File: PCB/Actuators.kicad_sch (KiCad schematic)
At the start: 90 parts, among them J1 R_Motor, J10 Servos, J11 PWR-Servos, J3 Left_Speaker, J4 Right_Speaker, J5 GAIN_sel, J6 L_Motor, J7 Servos, J8 Servos, J9 Servos, Q1 AOD417, U10 BTN7960B, U11 PCA9685PW, U2 MAX98357A, U4 MAX98357A, U5 BTN7960B, U6 BTN7960B, U7 74HC244, U8 74HC244, U9 BTN7960B

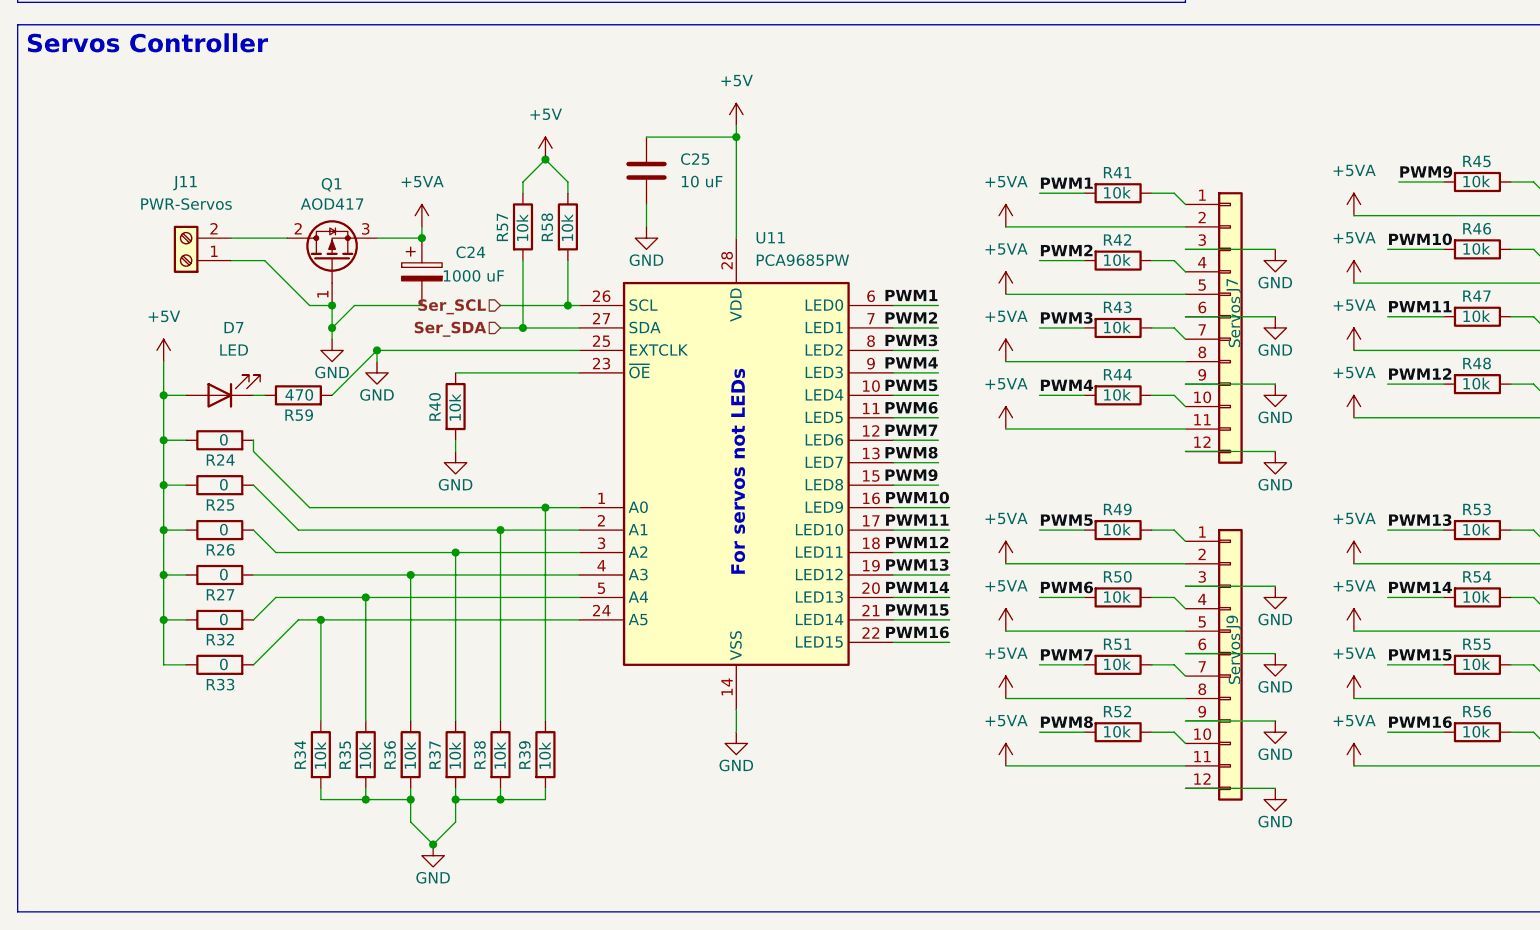
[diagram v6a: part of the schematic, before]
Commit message: [PCB] Traced motors controllers & step downs
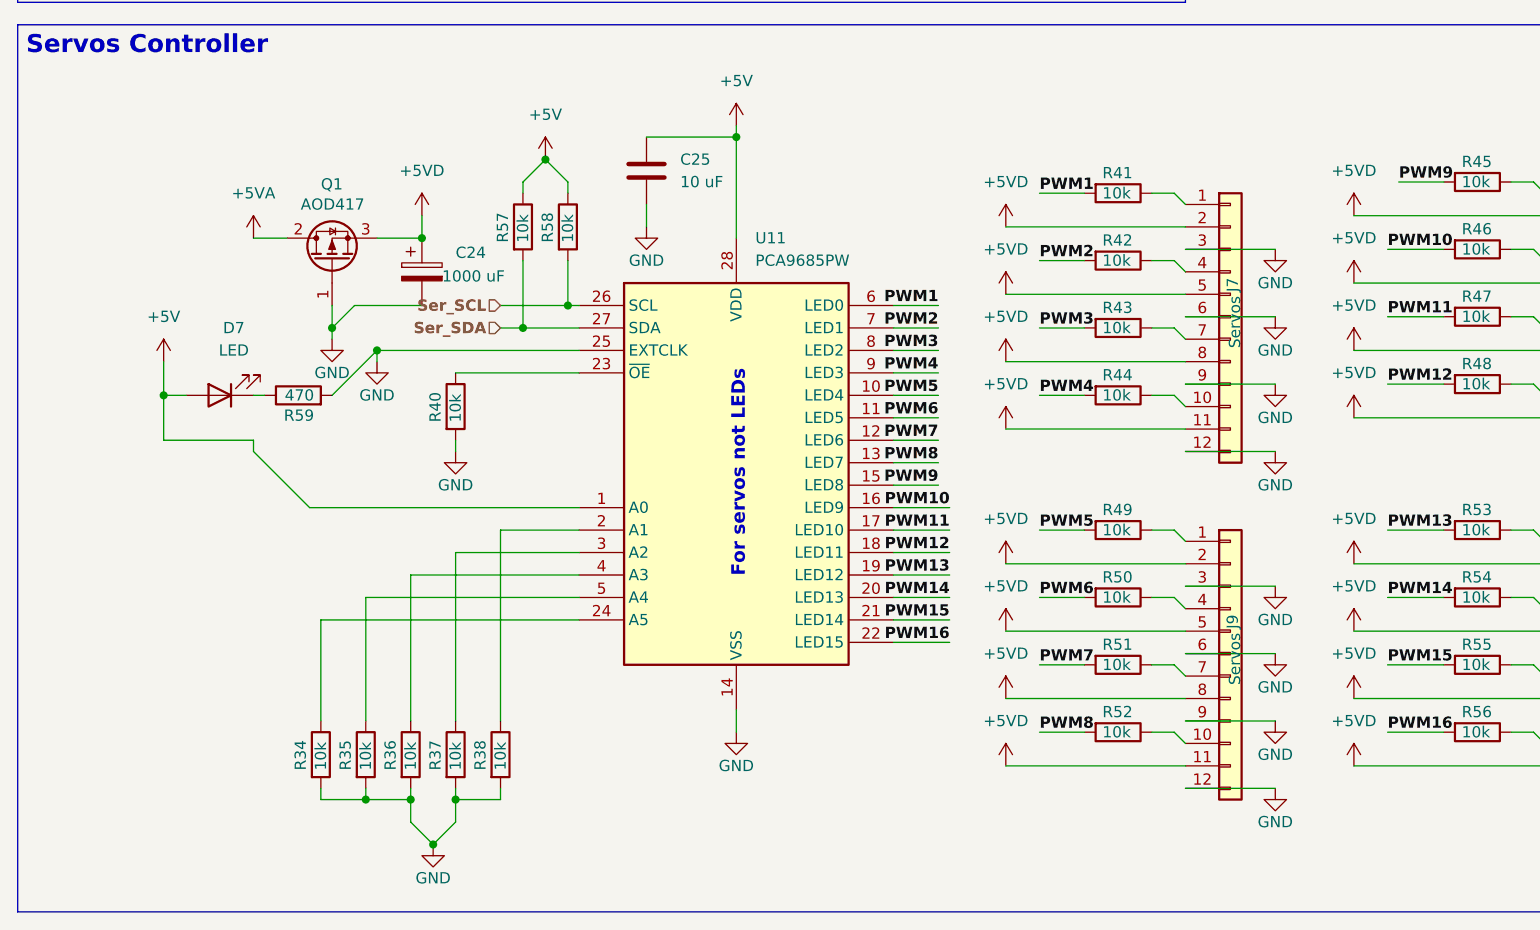
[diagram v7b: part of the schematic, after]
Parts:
- removed J11: PWR-Servos, TerminalBlock_Altech:Altech_AK100_1x02_P5.00mm, symbol Connector:Screw_Terminal_01x02
- removed R24, R25, R26, R27, R32, R33: 0, Resistor_SMD:R_0603_1608Metric_Pad0.98x0.95mm_HandSolder, symbol Device:R
- removed R39: 10k, Resistor_SMD:R_0603_1608Metric_Pad0.98x0.95mm_HandSolder, symbol Device:R
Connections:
- net +5V: now also U11.1 (A0)
- net +5VA: now also Q1.2 (D); no longer C24.1, J10.11 (Pin_11), J10.2 (Pin_2), J10.5 (Pin_5), J10.8 (Pin_8), J7.11 (Pin_11), J7.2 (Pin_2), J7.5 (Pin_5), J7.8 (Pin_8), J8.11 (Pin_11), J8.2 (Pin_2), J8.5 (Pin_5), J8.8 (Pin_8), J9.11 (Pin_11), J9.2 (Pin_2), J9.5 (Pin_5), J9.8 (Pin_8), Q1.3 (S)
- new net +5VD: C24.1, J10.11 (Pin_11), J10.2 (Pin_2), J10.5 (Pin_5), J10.8 (Pin_8), J7.11 (Pin_11), J7.2 (Pin_2), J7.5 (Pin_5), J7.8 (Pin_8), J8.11 (Pin_11), J8.2 (Pin_2), J8.5 (Pin_5), J8.8 (Pin_8), J9.11 (Pin_11), J9.2 (Pin_2), J9.5 (Pin_5), J9.8 (Pin_8), Q1.3 (S)

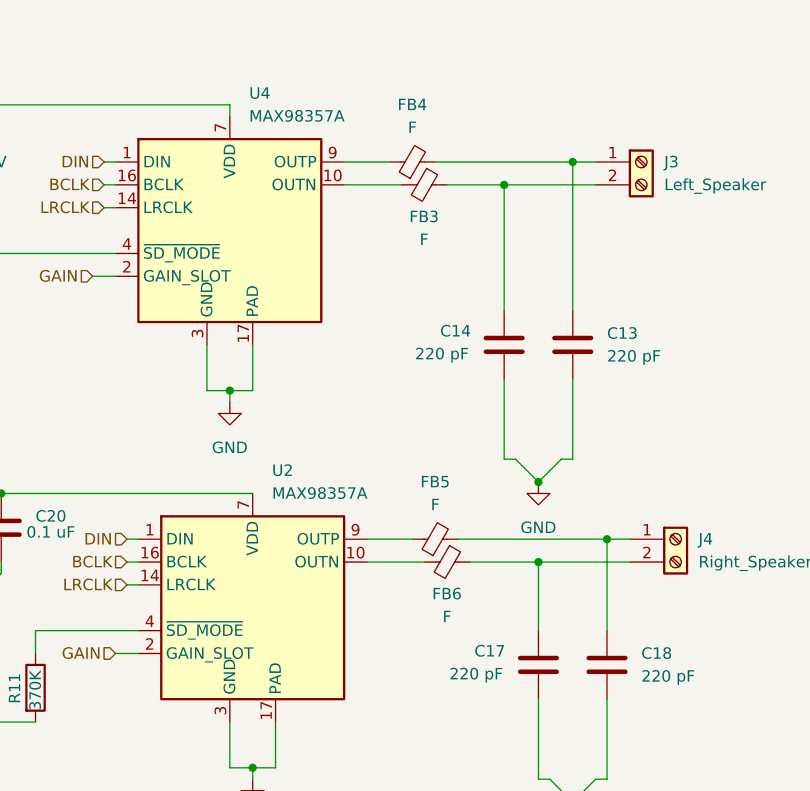
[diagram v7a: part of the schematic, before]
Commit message: [PCB] 95% finished the PCB
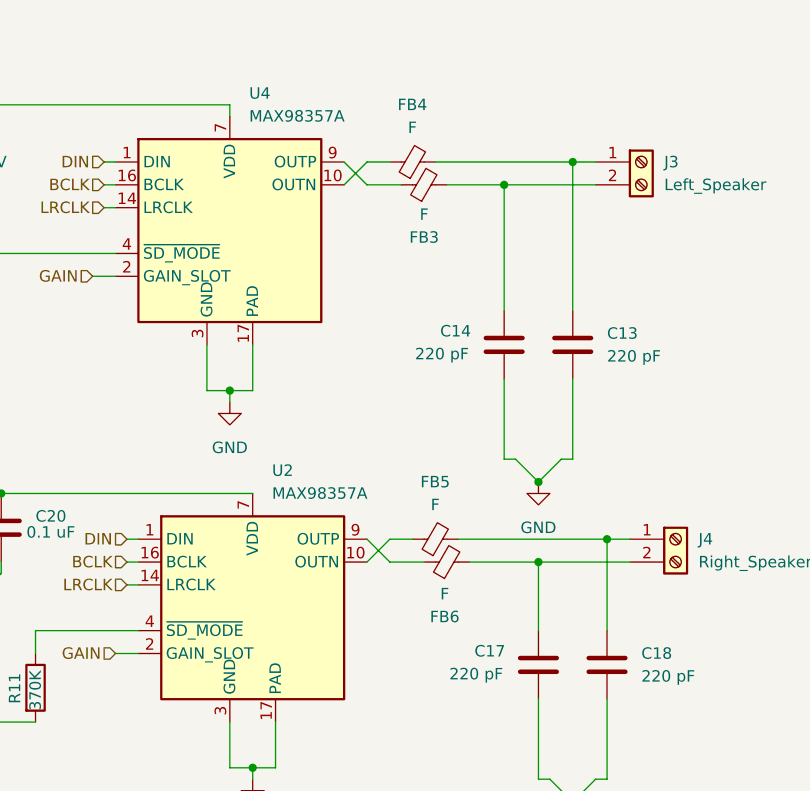
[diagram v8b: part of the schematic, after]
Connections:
- net at C14.2, J3.2 (Pin_2): now also FB3.2; no longer FB3.1
- net at U4.10 (OUTN): now also FB4.1; no longer FB3.2
- net at C17.2, J4.2 (Pin_2): now also FB6.2; no longer FB6.1
- net at U2.10 (OUTN): now also FB5.1; no longer FB6.2
- net at U4.9 (OUTP): now also FB3.1; no longer FB4.1
- net at U2.9 (OUTP): now also FB6.1; no longer FB5.1
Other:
- moved on the sheet: FB3, FB6
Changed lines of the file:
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@@
 	(wire
 		(pts
+			(xy 92.71 38.1) (xy 90.17 35.56)
+		)
+		(stroke
+			(width 0)
+			(type default)
+		)
+	)
+	(wire
+		(pts
 			(xy 95.25 129.54) (xy 95.25 130.81)
 		)
@@
 	(wire
 		(pts
-			(xy 90.17 35.56) (xy 95.25 35.56)
+			(xy 95.25 35.56) (xy 92.71 35.56)
 		)
 		(stroke
@@
 	(wire
 		(pts
+			(xy 99.06 80.01) (xy 95.25 80.01)
+		)
+		(stroke
+			(width 0)
+			(type default)
+		)
+	)
+	(wire
+		(pts
 			(xy 182.88 52.07) (xy 182.88 69.85)
 		)
@@
 	(wire
 		(pts
+			(xy 95.25 77.47) (xy 92.71 80.01)
+		)
+		(stroke
+			(width 0)
+			(type default)
+		)
+	)
+	(wire
+		(pts
 			(xy 186.69 196.85) (xy 196.85 196.85)
 		)
@@
 	(wire
 		(pts
-			(xy 92.71 77.47) (xy 97.79 77.47)
-		)
-		(stroke
-			(width 0)
-			(type default)
-		)
-	)
-	(wire
-		(pts
 			(xy 118.11 154.94) (xy 113.03 154.94)
 		)
@@
 	(wire
 		(pts
+			(xy 92.71 35.56) (xy 90.17 38.1)
+		)
+		(stroke
+			(width 0)
+			(type default)
+		)
+	)
+	(wire
+		(pts
 			(xy 142.24 190.5) (xy 144.78 190.5)
 		)
@@
 	(wire
 		(pts
+			(xy 96.52 38.1) (xy 92.71 38.1)
+		)
+		(stroke
+			(width 0)
+			(type default)
+		)
+	)
+	(wire
+		(pts
 			(xy 113.03 177.8) (xy 119.38 177.8)
 		)
@@
 	(wire
 		(pts
-			(xy 90.17 38.1) (xy 96.52 38.1)
-		)
-		(stroke
-			(width 0)
-			(type default)
-		)
-	)
-	(wire
-		(pts
 			(xy 441.96 57.15) (xy 443.23 57.15)
 		)
@@
 	(wire
 		(pts
+			(xy 97.79 77.47) (xy 95.25 77.47)
+		)
+		(stroke
+			(width 0)
+			(type default)
+		)
+	)
+	(wire
+		(pts
 			(xy 30.48 160.02) (xy 33.02 160.02)
 		)
@@
 	(wire
 		(pts
-			(xy 92.71 80.01) (xy 99.06 80.01)
-		)
-		(stroke
-			(width 0)
-			(type default)
-		)
-	)
-	(wire
-		(pts
 			(xy 186.69 189.23) (xy 196.85 189.23)
 		)
@@
 	(wire
 		(pts
+			(xy 95.25 80.01) (xy 92.71 77.47)
+		)
+		(stroke
+			(width 0)
+			(type default)
+		)
+	)
+	(wire
+		(pts
 			(xy 266.7 41.91) (xy 266.7 43.18)
 		)
@@
 	(symbol
 		(lib_id "Device:FerriteBead_Small")
-		(at 99.06 38.1 270)
+		(at 99.06 38.1 90)
 		(unit 1)
 		(body_style 1)
@@
 		(dnp no)
 		(property "Reference" "FB3"
-			(at 99.06 41.656 90)
+			(at 99.06 43.942 90)
 			(show_name no)
 			(do_not_autoplace no)
@@
 		)
 		(property "Value" "F"
-			(at 99.06 44.196 90)
+			(at 99.06 41.402 90)
 			(show_name no)
 			(do_not_autoplace no)
@@
 		)
 		(property "Footprint" "Capacitor_SMD:C_0603_1608Metric_Pad1.08x0.95mm_HandSolder"
-			(at 99.06 36.322 90)
+			(at 99.06 39.878 90)
 			(hide yes)
 			(show_name no)
@@
 	(symbol
 		(lib_id "Device:FerriteBead_Small")
-		(at 101.6 80.01 270)
+		(at 101.6 80.01 90)
 		(unit 1)
 		(body_style 1)
@@
 		(dnp no)
 		(property "Reference" "FB6"
-			(at 101.6 83.566 90)
+			(at 101.346 86.106 90)
 			(show_name no)
 			(do_not_autoplace no)
@@
 		)
 		(property "Value" "F"
-			(at 101.6 86.106 90)
+			(at 101.346 83.566 90)
 			(show_name no)
 			(do_not_autoplace no)
@@
 		)
 		(property "Footprint" "Capacitor_SMD:C_0603_1608Metric_Pad1.08x0.95mm_HandSolder"
-			(at 101.6 78.232 90)
+			(at 101.6 81.788 90)
 			(hide yes)
 			(show_name no)
